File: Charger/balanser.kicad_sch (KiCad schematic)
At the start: 68 parts, among them Q1 BC846BW, Q10 MJD45H11T4, Q11 MJD45H11T4, Q12 MJD45H11T4, Q2 BC846BW, Q3 BC846BW, Q4 MJD45H11T4, Q5 MJD45H11T4, Q6 MJD45H11T4, Q7 BC846BW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

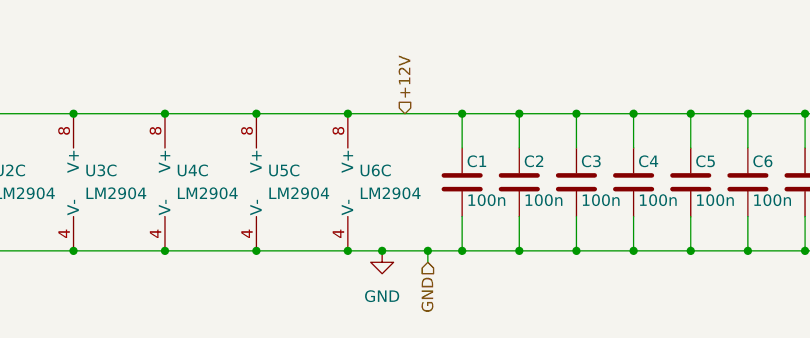
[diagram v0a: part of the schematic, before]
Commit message: update
zakonczony schemat balansera, sztucznego obciazenia i pomiaru pradu. Przypisane wszystkie footprinty
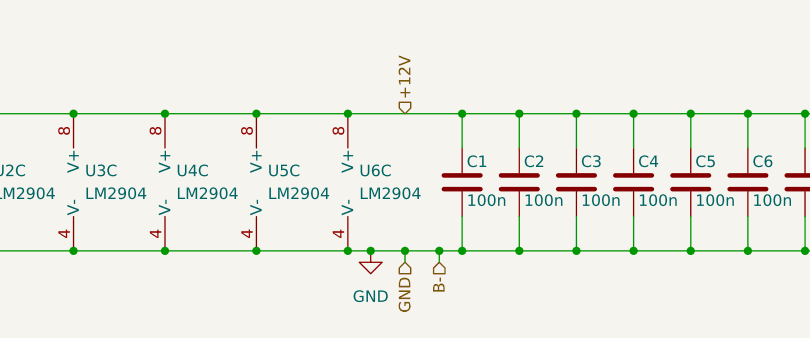
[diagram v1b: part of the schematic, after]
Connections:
- net B- is gone; now on net GND: Q12.2 (C), R27.1
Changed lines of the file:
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@@
 	)
 	(junction
+		(at 83.82 177.8)
+		(diameter 0)
+		(color 0 0 0 0)
+	)
+	(junction
 		(at 63.5 80.01)
 		(diameter 0)
@@
 	)
 	(junction
+		(at 91.44 177.8)
+		(diameter 0)
+		(color 0 0 0 0)
+	)
+	(junction
 		(at 40.64 162.56)
 		(diameter 0)
@@
 	)
 	(junction
+		(at 87.63 177.8)
+		(diameter 0)
+		(color 0 0 0 0)
+	)
+	(junction
 		(at 125.73 177.8)
 		(diameter 0)
@@
 	)
 	(junction
-		(at 90.17 177.8)
-		(diameter 0)
-		(color 0 0 0 0)
-	)
-	(junction
 		(at 172.72 78.74)
 		(diameter 0)
@@
 	)
 	(junction
-		(at 85.09 177.8)
-		(diameter 0)
-		(color 0 0 0 0)
-	)
-	(junction
 		(at 63.5 72.39)
 		(diameter 0)
@@
 	(wire
 		(pts
-			(xy 85.09 177.8) (xy 90.17 177.8)
+			(xy 83.82 177.8) (xy 87.63 177.8)
 		)
 		(stroke
@@
 	(wire
 		(pts
-			(xy 90.17 177.8) (xy 90.17 179.07)
+			(xy 87.63 177.8) (xy 87.63 179.07)
 		)
 		(stroke
@@
 	(wire
 		(pts
+			(xy 91.44 177.8) (xy 91.44 179.07)
+		)
+		(stroke
+			(width 0)
+			(type default)
+		)
+	)
+	(wire
+		(pts
 			(xy 113.03 173.99) (xy 113.03 177.8)
 		)
@@
 	(wire
 		(pts
-			(xy 90.17 177.8) (xy 93.98 177.8)
+			(xy 87.63 177.8) (xy 91.44 177.8)
 		)
 		(stroke
@@
 	(wire
 		(pts
-			(xy 81.28 177.8) (xy 85.09 177.8)
+			(xy 81.28 177.8) (xy 83.82 177.8)
 		)
 		(stroke
@@
 	(wire
 		(pts
+			(xy 91.44 177.8) (xy 93.98 177.8)
+		)
+		(stroke
+			(width 0)
+			(type default)
+		)
+	)
+	(wire
+		(pts
 			(xy 48.26 72.39) (xy 48.26 77.47)
 		)
@@
 	(hierarchical_label "GND"
 		(shape input)
-		(at 90.17 179.07 270)
+		(at 87.63 179.07 270)
 		(fields_autoplaced yes)
 		(effects
@@
 		)
 	)
+	(hierarchical_label "B-"
+		(shape input)
+		(at 91.44 179.07 270)
+		(fields_autoplaced yes)
+		(effects
+			(font
+				(size 1.27 1.27)
+			)
+			(justify right)
+		)
+	)
 	(hierarchical_label "V_bat_4"
 		(shape output)
@@
 	(symbol
 		(lib_id "power:GND")
-		(at 85.09 177.8 0)
+		(at 83.82 177.8 0)
 		(unit 1)
 		(exclude_from_sim no)
@@
 		(fields_autoplaced yes)
 		(property "Reference" "#PWR012"
-			(at 85.09 184.15 0)
+			(at 83.82 184.15 0)
 			(effects
 				(font
@@
 		)
 		(property "Value" "GND"
-			(at 85.09 182.88 0)
+			(at 83.82 182.88 0)
 			(effects
 				(font
@@
 		)
 		(property "Footprint" ""
-			(at 85.09 177.8 0)
+			(at 83.82 177.8 0)
 			(effects
 				(font
@@
 		)
 		(property "Datasheet" ""
-			(at 85.09 177.8 0)
+			(at 83.82 177.8 0)
 			(effects
 				(font
@@
 		)
 		(property "Description" "Power symbol creates a global label with name \"GND\" , ground"
-			(at 85.09 177.8 0)
+			(at 83.82 177.8 0)
 			(effects
 				(font

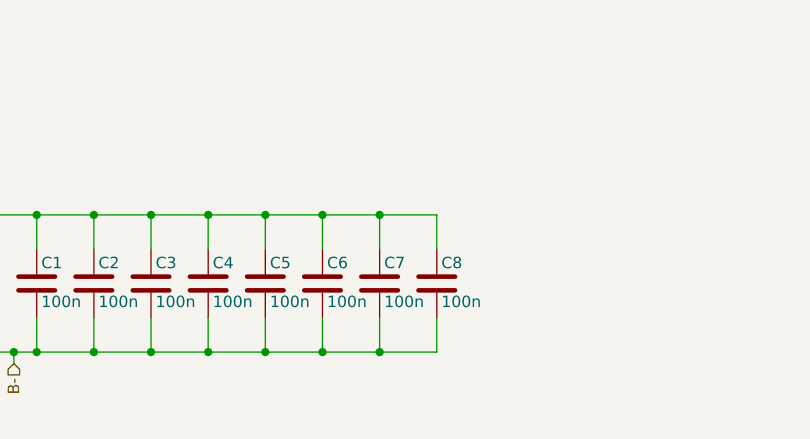
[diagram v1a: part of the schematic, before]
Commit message: obrocone zlacze balansera
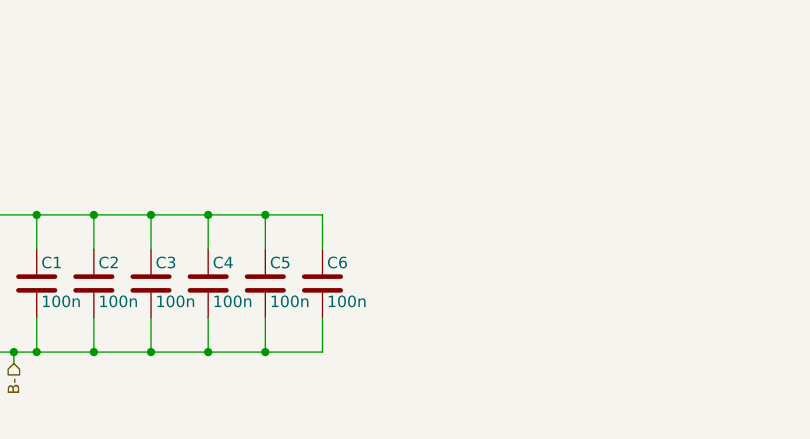
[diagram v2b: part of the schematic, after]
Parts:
- removed C7, C8: 100n, Capacitor_SMD:C_0805_2012Metric_Pad1.18x1.45mm_HandSolder, symbol Device:C
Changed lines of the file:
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@@
 	)
 	(junction
-		(at 125.73 177.8)
-		(diameter 0)
-		(color 0 0 0 0)
-	)
-	(junction
 		(at 187.96 109.22)
 		(diameter 0)
@@
 	)
 	(junction
-		(at 132.08 162.56)
-		(diameter 0)
-		(color 0 0 0 0)
-	)
-	(junction
-		(at 125.73 162.56)
-		(diameter 0)
-		(color 0 0 0 0)
-	)
-	(junction
-		(at 132.08 177.8)
-		(diameter 0)
-		(color 0 0 0 0)
-	)
-	(junction
 		(at 92.71 118.11)
 		(diameter 0)
@@
 	(wire
 		(pts
-			(xy 132.08 162.56) (xy 132.08 166.37)
-		)
-		(stroke
-			(width 0)
-			(type default)
-		)
-	)
-	(wire
-		(pts
 			(xy 172.72 109.22) (xy 172.72 114.3)
 		)
@@
 	(wire
 		(pts
-			(xy 132.08 162.56) (xy 138.43 162.56)
-		)
-		(stroke
-			(width 0)
-			(type default)
-		)
-	)
-	(wire
-		(pts
 			(xy 172.72 83.82) (xy 171.45 83.82)
 		)
@@
 	(wire
 		(pts
-			(xy 125.73 177.8) (xy 132.08 177.8)
-		)
-		(stroke
-			(width 0)
-			(type default)
-		)
-	)
-	(wire
-		(pts
 			(xy 190.5 49.53) (xy 190.5 54.61)
 		)
@@
 	(wire
 		(pts
-			(xy 132.08 177.8) (xy 138.43 177.8)
-		)
-		(stroke
-			(width 0)
-			(type default)
-		)
-	)
-	(wire
-		(pts
 			(xy 46.99 113.03) (xy 48.26 113.03)
 		)
@@
 	(wire
 		(pts
-			(xy 125.73 162.56) (xy 132.08 162.56)
-		)
-		(stroke
-			(width 0)
-			(type default)
-		)
-	)
-	(wire
-		(pts
 			(xy 119.38 177.8) (xy 125.73 177.8)
 		)
@@
 	(wire
 		(pts
-			(xy 138.43 177.8) (xy 138.43 173.99)
-		)
-		(stroke
-			(width 0)
-			(type default)
-		)
-	)
-	(wire
-		(pts
-			(xy 132.08 173.99) (xy 132.08 177.8)
-		)
-		(stroke
-			(width 0)
-			(type default)
-		)
-	)
-	(wire
-		(pts
 			(xy 171.45 114.3) (xy 172.72 114.3)
 		)
@@
 	(wire
 		(pts
-			(xy 138.43 162.56) (xy 138.43 166.37)
-		)
-		(stroke
-			(width 0)
-			(type default)
-		)
-	)
-	(wire
-		(pts
 			(xy 119.38 173.99) (xy 119.38 177.8)
 		)
@@
 	)
 	(symbol
-		(lib_id "Device:C")
-		(at 138.43 170.18 0)
-		(unit 1)
-		(exclude_from_sim no)
-		(in_bom yes)
-		(on_board yes)
-		(dnp no)
-		(property "Reference" "C8"
-			(at 138.938 167.894 0)
-			(effects
-				(font
-					(size 1.27 1.27)
-				)
-				(justify left)
-			)
-		)
-		(property "Value" "100n"
-			(at 138.938 172.212 0)
-			(effects
-				(font
-					(size 1.27 1.27)
-				)
-				(justify left)
-			)
-		)
-		(property "Footprint" "Capacitor_SMD:C_0805_2012Metric_Pad1.18x1.45mm_HandSolder"
-			(at 139.3952 173.99 0)
-			(effects
-				(font
-					(size 1.27 1.27)
-				)
-				(hide yes)
-			)
-		)
-		(property "Datasheet" "~"
-			(at 138.43 170.18 0)
-			(effects
-				(font
-					(size 1.27 1.27)
-				)
-				(hide yes)
-			)
-		)
-		(property "Description" "Unpolarized capacitor"
-			(at 138.43 170.18 0)
-			(effects
-				(font
-					(size 1.27 1.27)
-				)
-				(hide yes)
-			)
-		)
-		(pin "2"
-		)
-		(pin "1"
-		)
-		(instances
-			(project "Charger"
-				(path "/f0501846-9b00-4ec1-8596-952177c35a04/0f0bd340-c2d3-48dd-bd01-ac817c0395cc"
-					(reference "C8")
-					(unit 1)
-				)
-			)
-		)
-	)
-	(symbol
 		(lib_id "Device:R")
 		(at 46.99 87.63 0)
@@
 					(unit 1)
 				)
-			)
-		)
-	)
-	(symbol
-		(lib_id "Device:C")
-		(at 132.08 170.18 0)
-		(unit 1)
-		(exclude_from_sim no)
-		(in_bom yes)
-		(on_board yes)
-		(dnp no)
-		(property "Reference" "C7"
-			(at 132.588 167.894 0)
-			(effects
-				(font
-					(size 1.27 1.27)
-				)
-				(justify left)
-			)
-		)
-		(property "Value" "100n"
-			(at 132.588 172.212 0)
-			(effects
-				(font
-					(size 1.27 1.27)
-				)
-				(justify left)
-			)
-		)
-		(property "Footprint" "Capacitor_SMD:C_0805_2012Metric_Pad1.18x1.45mm_HandSolder"
-			(at 133.0452 173.99 0)
-			(effects
-				(font
-					(size 1.27 1.27)
-				)
-				(hide yes)
-			)
-		)
-		(property "Datasheet" "~"
-			(at 132.08 170.18 0)
-			(effects
-				(font
-					(size 1.27 1.27)
-				)
-				(hide yes)
-			)
-		)
-		(property "Description" "Unpolarized capacitor"
-			(at 132.08 170.18 0)
-			(effects
-				(font
-					(size 1.27 1.27)
-				)
-				(hide yes)
-			)
-		)
-		(pin "2"
-		)
-		(pin "1"
-		)
-		(instances
-			(project "Charger"
-				(path "/f0501846-9b00-4ec1-8596-952177c35a04/0f0bd340-c2d3-48dd-bd01-ac817c0395cc"
-					(reference "C7")
-					(unit 1)
-				)

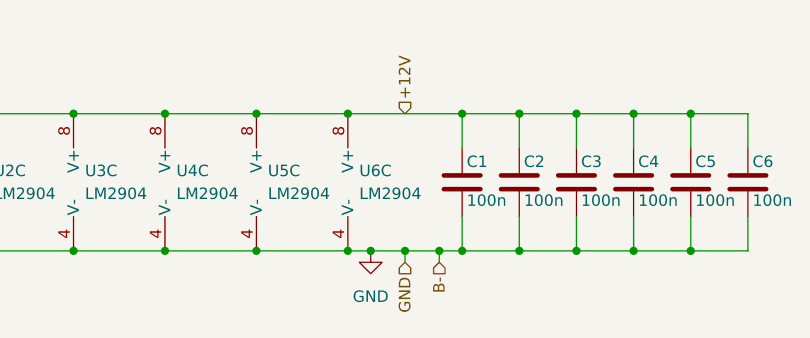
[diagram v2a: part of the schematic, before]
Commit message: dodana ladowarka do glownego projektu
drobne zmiany w sumie wszedzie pozbyłem sie 3.3v poza sterowaniem z pinów mcu, dopiescilem rezystorki zby bylo jak najmniej wartości rozszerzylem delikatnie zakres pradowy przetwornicy
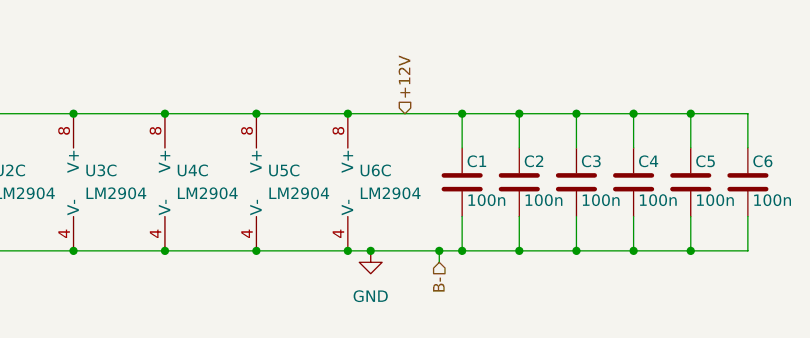
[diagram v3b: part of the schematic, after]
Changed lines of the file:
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@@
-	)
-	(junction
-		(at 87.63 177.8)
-		(diameter 0)
-		(color 0 0 0 0)
 	)
 	(junction
@@
 	(wire
 		(pts
-			(xy 83.82 177.8) (xy 87.63 177.8)
+			(xy 83.82 177.8) (xy 91.44 177.8)
 		)
 		(stroke
@@
 	(wire
 		(pts
-			(xy 87.63 177.8) (xy 87.63 179.07)
-		)
-		(stroke
-			(width 0)
-			(type default)
-		)
-	)
-	(wire
-		(pts
 			(xy 63.5 69.85) (xy 63.5 72.39)
 		)
@@
 	(wire
 		(pts
-			(xy 87.63 177.8) (xy 91.44 177.8)
-		)
-		(stroke
-			(width 0)
-			(type default)
-		)
-	)
-	(wire
-		(pts
 			(xy 125.73 162.56) (xy 125.73 166.37)
 		)
@@
 		)
 	)
-	(hierarchical_label "GND"
-		(shape input)
-		(at 87.63 179.07 270)
-		(fields_autoplaced yes)
-		(effects
-			(font
-				(size 1.27 1.27)
-			)
-			(justify right)
-		)
-	)
